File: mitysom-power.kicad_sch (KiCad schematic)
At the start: 23 parts, among them J2201 Plug_Samtec_SEAM-50-02.0-L-08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, J2202 PinHeader_1x3_P2.54mm_Drill1.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

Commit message: [#100282] Reorder schematic pages, reannotate schematic
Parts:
- renumbered BT2201 to BT101, C2213 to C101, C2216 to C102, C2214 to C103, C2217 to C104, C2201 to C105, C2202 to C106, C2203 to C107, C2204 to C108, C2205 to C109, C2206 to C110, C2209 to C111, C2212 to C112, C2215 to C113, C2218 to C114, C2207 to C115, C2210 to C116, C2208 to C117, C2211 to C118, J2201 to J101, J2202 to J102, R2201 to R101, TP2201 to TP101

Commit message: [#100282] Change SoM connector designator to J100
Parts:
- renumbered J101 to J100
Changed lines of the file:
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@@
 		(dnp no)
 		(fields_autoplaced yes)
-		(property "Reference" "J101"
+		(property "Reference" "J100"
 			(at 311.15 73.66 0)
 			(show_name no)
@@
 			(project "altera-modular-agilex-5-dc-scm"
 				(path "/6bb9d978-a328-4b30-874b-55170a976185/ccfd355f-9460-404d-be61-24db575a0371"
-					(reference "J101")
+					(reference "J100")
 					(unit 9)
 				)
@@
 		(dnp no)
 		(fields_autoplaced yes)
-		(property "Reference" "J101"
+		(property "Reference" "J100"
 			(at 151.765 146.05 0)
 			(show_name no)
@@
 			(project "altera-modular-agilex-5-dc-scm"
 				(path "/6bb9d978-a328-4b30-874b-55170a976185/ccfd355f-9460-404d-be61-24db575a0371"
-					(reference "J101")
+					(reference "J100")
 					(unit 1)
 				)

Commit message: [#100282] Connect signals to HVIO banks
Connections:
- net +1V8: now also C113.2, C114.2, J100.[D15,D16] (VCCIO_6C6D)
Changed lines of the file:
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@@
+	)
+	(symbol
+		(lib_id "power:+1V8")
+		(at 212.09 142.24 0)
+		(unit 1)
+		(body_style 1)
+		(exclude_from_sim no)
+		(in_bom yes)
+		(on_board yes)
+		(in_pos_files yes)
+		(dnp no)
+		(property "Reference" "#PWR0129"
+			(at 212.09 146.05 0)
+			(hide yes)
+			(show_name no)
+			(do_not_autoplace no)
+			(effects
+				(font
+					(size 1.27 1.27)
+				)
+			)
+		)
+		(property "Value" "+1V8"
+			(at 212.09 138.43 0)
+			(show_name no)
+			(do_not_autoplace no)
+			(effects
+				(font
+					(size 1.27 1.27)
+				)
+			)
+		)
+		(property "Footprint" ""
+			(at 212.09 142.24 0)
+			(hide yes)
+			(show_name no)
+			(do_not_autoplace no)
+			(effects
+				(font
+					(size 1.27 1.27)
+				)
+			)
+		)
+		(property "Datasheet" ""
+			(at 212.09 142.24 0)
+			(hide yes)
+			(show_name no)
+			(do_not_autoplace no)
+			(effects
+				(font
+					(size 1.27 1.27)
+				)
+			)
+		)
+		(property "Description" "Power symbol creates a global label with name \"+1V8\""
+			(at 212.09 142.24 0)
+			(hide yes)
+			(show_name no)
+			(do_not_autoplace no)
+			(effects
+				(font
+					(size 1.27 1.27)
+				)
+			)
+		)
+		(pin "1"
+		)
+		(instances
+			(project "altera-modular-agilex-5-dc-scm"
+				(path "/6bb9d978-a328-4b30-874b-55170a976185/ccfd355f-9460-404d-be61-24db575a0371"
+					(reference "#PWR0129")
+					(unit 1)
+				)
+			)
+		)
 	)
 	(symbol

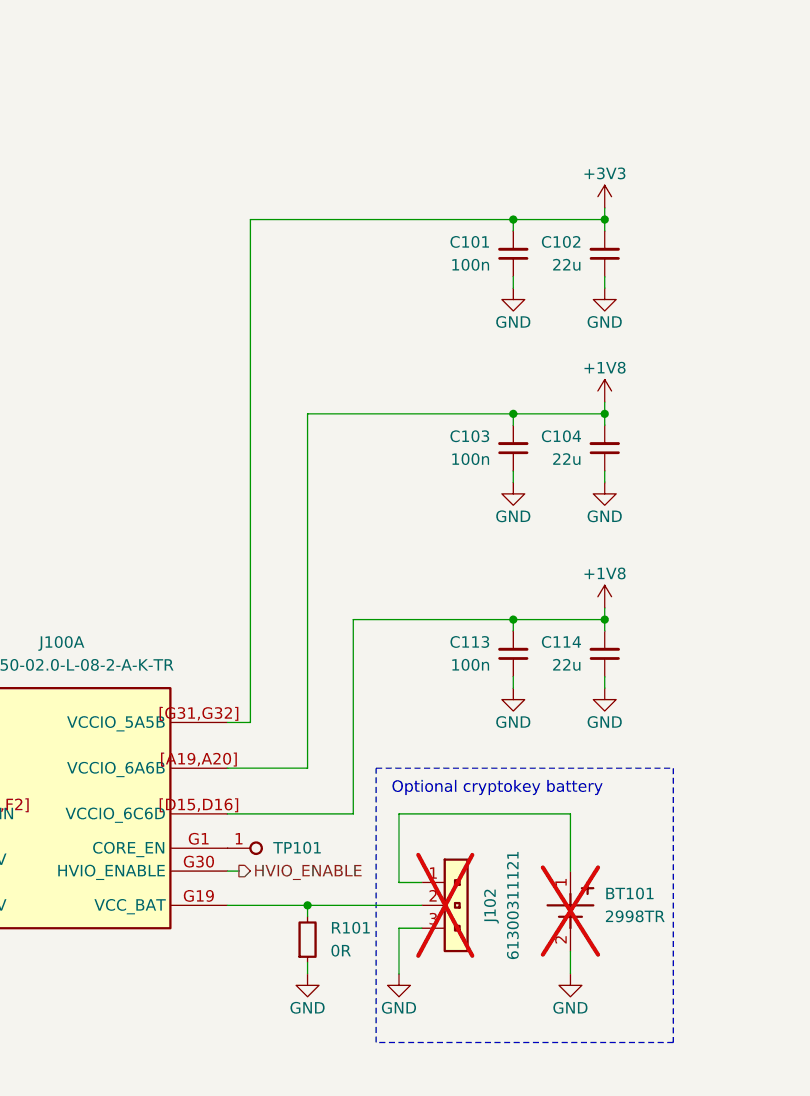
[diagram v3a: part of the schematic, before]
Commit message: [#100282] Swap TMP default from QSPI to SPI, add level shifter for PECI I2C bus, connect user button
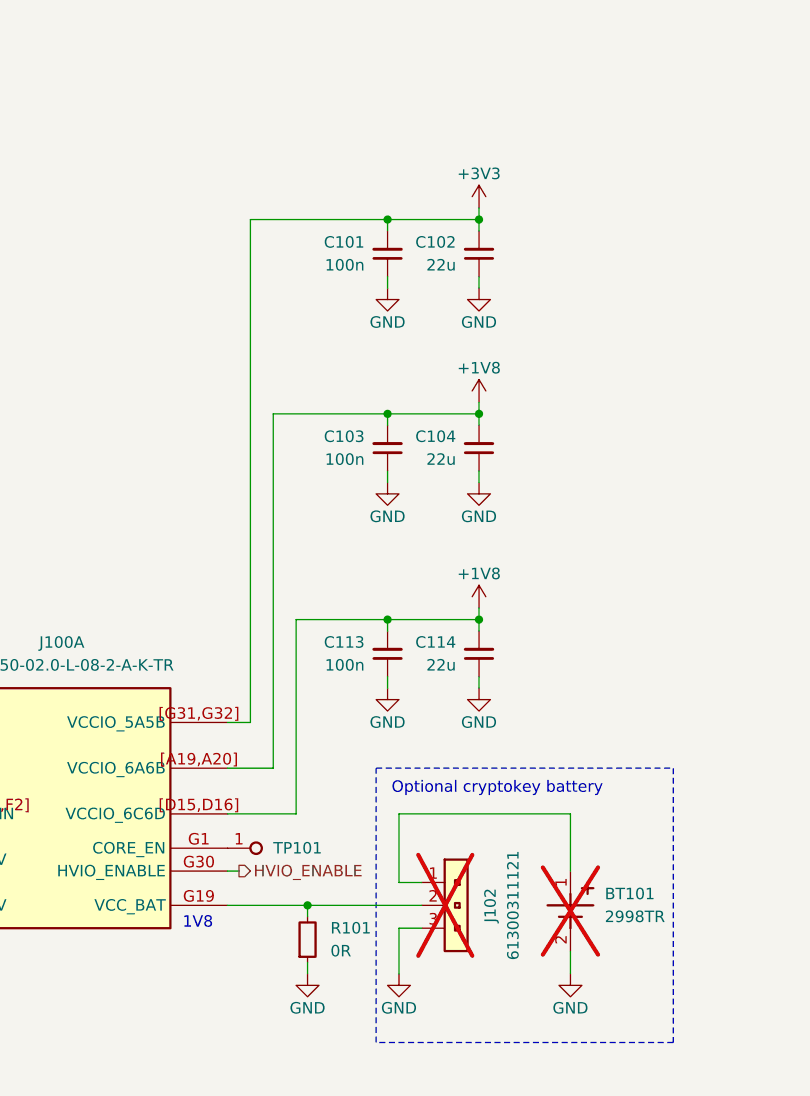
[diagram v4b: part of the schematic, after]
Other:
- note added: "1V8"
- moved on the sheet: C101, C102, C103, C104, C113, C114

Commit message: [#100282] Update components from library
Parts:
- C105, C106, C107, C108: Public False -> (none)
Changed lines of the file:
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@@
 			)
 		)
-		(property "Description" "Power symbol creates a global label with name \"+1V8\""
+		(property "Description" ""
 			(at 213.36 132.08 0)
 			(hide yes)
@@
 			)
 		)
-		(property "Public" "False"
-			(at 105.41 127 0)
-			(hide yes)
-			(show_name no)
-			(do_not_autoplace no)
-			(effects
-				(font
-					(size 1.27 1.27)
-				)
-				(justify left bottom)
-			)
-		)
 		(pin "2"
 		)
@@
 			)
 		)
-		(property "Public" "False"
-			(at 114.3 127 0)
-			(hide yes)
-			(show_name no)
-			(do_not_autoplace no)
-			(effects
-				(font
-					(size 1.27 1.27)
-				)
-				(justify left bottom)
-			)
-		)
 		(pin "2"
 		)
@@
 			)
 		)
-		(property "Public" "False"
-			(at 96.52 127 0)
-			(hide yes)
-			(show_name no)
-			(do_not_autoplace no)
-			(effects
-				(font
-					(size 1.27 1.27)
-				)
-				(justify left bottom)
-			)
-		)
 		(pin "2"
 		)
@@
 			)
 		)
-		(property "Description" "Power symbol creates a global label with name \"+1V8\""
+		(property "Description" ""
 			(at 213.36 154.94 0)
 			(hide yes)
@@
 			(hide yes)
 			(show_name no)
-			(do_not_autoplace no)
-			(effects
-				(font
-					(size 1.27 1.27)
-				)
-				(justify left bottom)
-			)
-		)
-		(property "Public" "False"
-			(at 87.63 127 0)
-			(hide yes)
-			(show_name no)

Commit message: [#100282] Update selected symbols
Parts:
- C105, C106, C107, C108: Public (none) -> False
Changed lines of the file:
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@@
 			)
 		)
+		(property "Public" "False"
+			(at 105.41 127 0)
+			(hide yes)
+			(show_name no)
+			(do_not_autoplace no)
+			(effects
+				(font
+					(size 1.27 1.27)
+				)
+				(justify left bottom)
+			)
+		)
 		(pin "2"
 		)
@@
 			)
 		)
+		(property "Public" "False"
+			(at 114.3 127 0)
+			(hide yes)
+			(show_name no)
+			(do_not_autoplace no)
+			(effects
+				(font
+					(size 1.27 1.27)
+				)
+				(justify left bottom)
+			)
+		)
 		(pin "2"
 		)
@@
 	)
 	(symbol
-		(lib_id "power:GND")
+		(lib_id "antmicropower:GND")
 		(at 208.28 182.88 0)
 		(unit 1)
@@
 			)
 		)
+		(property "Author" "Antmicro"
+			(at 217.17 190.5 0)
+			(hide yes)
+			(show_name no)
+			(do_not_autoplace no)
+			(effects
+				(font
+					(size 1.27 1.27)
+					(thickness 0.15)
+				)
+				(justify left bottom)
+			)
+		)
+		(property "License" "Apache-2.0"
+			(at 217.17 193.04 0)
+			(hide yes)
+			(show_name no)
+			(do_not_autoplace no)
+			(effects
+				(font
+					(size 1.27 1.27)
+					(thickness 0.15)
+				)
+				(justify left bottom)
+			)
+		)
 		(pin "1"
 		)
@@
 	)
 	(symbol
-		(lib_id "power:GND")
+		(lib_id "antmicropower:GND")
 		(at 189.23 182.88 0)
 		(unit 1)
@@
 			)
 		)
+		(property "Author" "Antmicro"
+			(at 198.12 190.5 0)
+			(hide yes)
+			(show_name no)
+			(do_not_autoplace no)
+			(effects
+				(font
+					(size 1.27 1.27)
+					(thickness 0.15)
+				)
+				(justify left bottom)
+			)
+		)
+		(property "License" "Apache-2.0"
+			(at 198.12 193.04 0)
+			(hide yes)
+			(show_name no)
+			(do_not_autoplace no)
+			(effects
+				(font
+					(size 1.27 1.27)
+					(thickness 0.15)
+				)
+				(justify left bottom)
+			)
+		)
 		(pin "1"
 		)
@@
 			)
 		)
+		(property "Public" "False"
+			(at 96.52 127 0)
+			(hide yes)
+			(show_name no)
+			(do_not_autoplace no)
+			(effects
+				(font
+					(size 1.27 1.27)
+				)
+				(justify left bottom)
+			)
+		)
 		(pin "2"
 		)
@@
 	)
 	(symbol
-		(lib_id "power:GND")
+		(lib_id "antmicropower:GND")
 		(at 179.07 182.88 0)
 		(unit 1)
@@
 			)
 		)
+		(property "Author" "Antmicro"
+			(at 187.96 190.5 0)
+			(hide yes)
+			(show_name no)
+			(do_not_autoplace no)
+			(effects
+				(font
+					(size 1.27 1.27)
+					(thickness 0.15)
+				)
+				(justify left bottom)
+			)
+		)
+		(property "License" "Apache-2.0"
+			(at 187.96 193.04 0)
+			(hide yes)
+			(show_name no)
+			(do_not_autoplace no)
+			(effects
+				(font
+					(size 1.27 1.27)
+					(thickness 0.15)
+				)
+				(justify left bottom)
+			)
+		)
 		(pin "1"
 		)
@@
 			(hide yes)
 			(show_name no)
+			(do_not_autoplace no)
+			(effects
+				(font
+					(size 1.27 1.27)
+				)
+				(justify left bottom)
+			)
+		)
+		(property "Public" "False"
+			(at 87.63 127 0)
+			(hide yes)
+			(show_name no)

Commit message: [#100282] Clear ERC
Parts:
- C105, C106, C107, C108: Public False -> (none)
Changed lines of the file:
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@@
 			)
 		)
-		(property "Public" "False"
-			(at 105.41 127 0)
-			(hide yes)
-			(show_name no)
-			(do_not_autoplace no)
-			(effects
-				(font
-					(size 1.27 1.27)
-				)
-				(justify left bottom)
-			)
-		)
 		(pin "2"
 		)
@@
 			)
 		)
-		(property "Public" "False"
-			(at 114.3 127 0)
-			(hide yes)
-			(show_name no)
-			(do_not_autoplace no)
-			(effects
-				(font
-					(size 1.27 1.27)
-				)
-				(justify left bottom)
-			)
-		)
 		(pin "2"
 		)
@@
 			)
 		)
-		(property "Description" "Power symbol creates a global label with name \"GND\" , ground"
+		(property "Description" ""
 			(at 208.28 182.88 0)
 			(hide yes)
@@
 			)
 		)
-		(property "Description" "Power symbol creates a global label with name \"GND\" , ground"
+		(property "Description" ""
 			(at 189.23 182.88 0)
 			(hide yes)
@@
 			)
 		)
-		(property "Public" "False"
-			(at 96.52 127 0)
-			(hide yes)
-			(show_name no)
-			(do_not_autoplace no)
-			(effects
-				(font
-					(size 1.27 1.27)
-				)
-				(justify left bottom)
-			)
-		)
 		(pin "2"
 		)
@@
 			)
 		)
-		(property "Description" "Power symbol creates a global label with name \"GND\" , ground"
+		(property "Description" ""
 			(at 179.07 182.88 0)
 			(hide yes)
@@
 			(hide yes)
 			(show_name no)
-			(do_not_autoplace no)
-			(effects
-				(font
-					(size 1.27 1.27)
-				)
-				(justify left bottom)
-			)
-		)
-		(property "Public" "False"
-			(at 87.63 127 0)
-			(hide yes)
-			(show_name no)
